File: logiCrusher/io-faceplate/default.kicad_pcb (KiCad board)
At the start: 2 copper layers, 40 x 129 mm, 0 parts

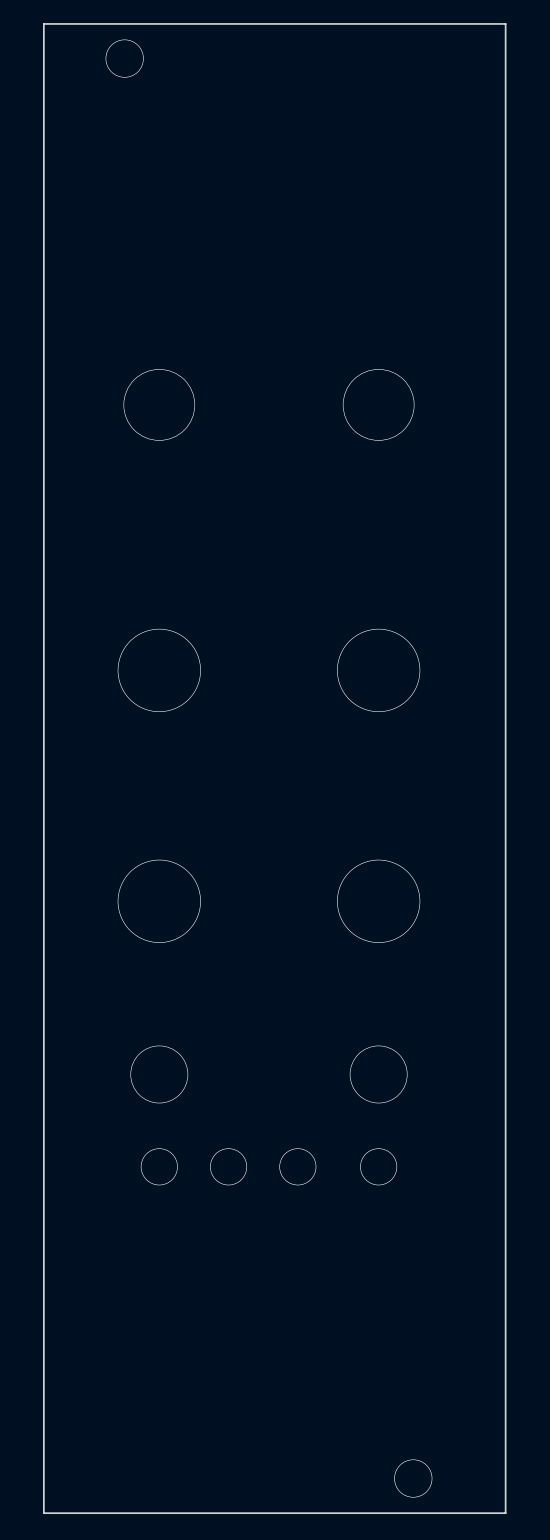
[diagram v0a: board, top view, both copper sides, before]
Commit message: Fit check on the drum and logiccrusher
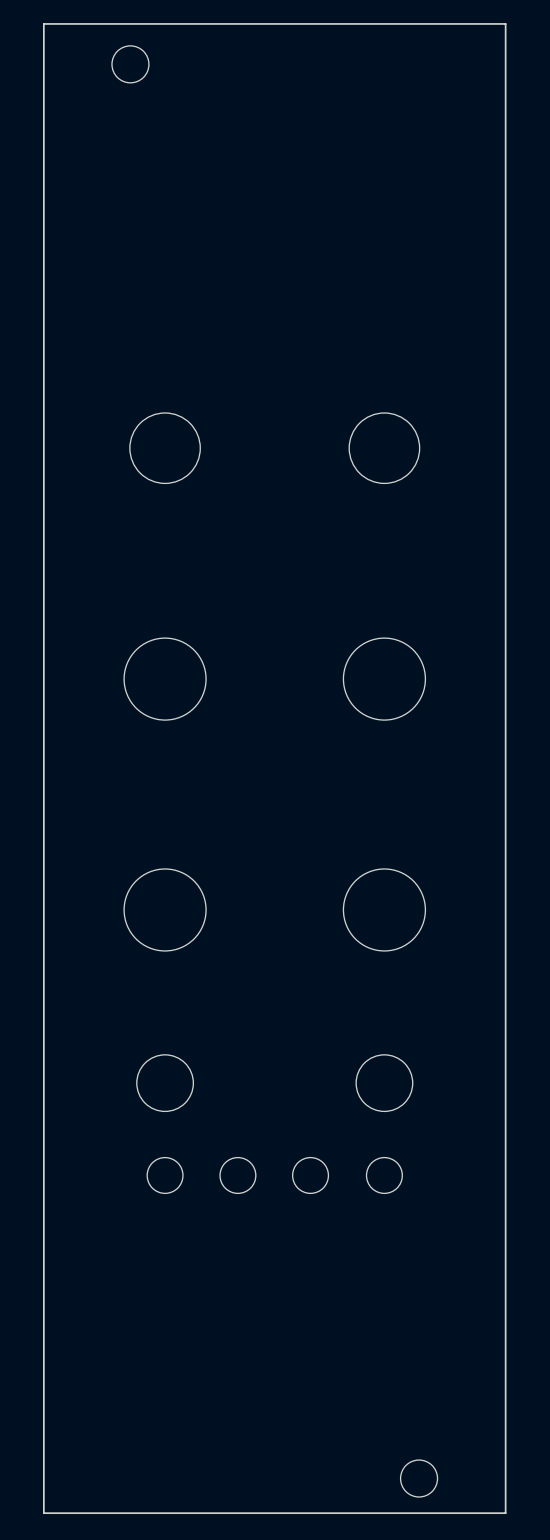
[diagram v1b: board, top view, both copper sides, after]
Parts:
- added ?: , MountingHole:MountingHole_3.5mm, F.Cu at (157.5, 24.5)
- added ?: , MountingHole:MountingHole_3.5mm, F.Cu at (166.8, 120.8)
- added ?: , MountingHole:MountingHole_3.5mm, F.Cu at (173.1, 120.8)
- added ?: , MountingHole:MountingHole_3.5mm, F.Cu at (179.5, 120.8)
- added ?: , MountingHole:MountingHole_3.5mm, F.Cu at (160.5, 112.8)
- added ?: , MountingHole:MountingHole_3.5mm, F.Cu at (179.5, 112.8)
- added ?: , MountingHole:MountingHole_3.5mm, F.Cu at (182.5, 147.0)
- added ?: , MountingHole:MountingHole_3.5mm, F.Cu at (160.5, 97.8)
- added ?: , MountingHole:MountingHole_3.5mm, F.Cu at (179.5, 97.8)
- added ?: , MountingHole:MountingHole_3.5mm, F.Cu at (160.5, 77.8)
- added ?: , MountingHole:MountingHole_3.5mm, F.Cu at (179.5, 77.8)
- added ?: , MountingHole:MountingHole_3.5mm, F.Cu at (160.5, 57.8)
- added ?: , MountingHole:MountingHole_3.5mm, F.Cu at (179.5, 57.8)
- added ?: , MountingHole:MountingHole_3.5mm, F.Cu at (160.5, 120.8)
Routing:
- net (no net): vias 14 -> 0
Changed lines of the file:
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@@
-(kicad_pcb (version 20171130) (host pcbnew 5.0.2+dfsg1-1~bpo9+1)
+(kicad_pcb (version 20171130) (host pcbnew "(5.0.2)-1")
   (general
     (thickness 1.6)
-    (drawings 10)
-    (tracks 14)
+    (drawings 4)
+    (tracks 0)
     (zones 0)
     (modules 0)
@@
       (outputformat 1)
       (mirror false)
-      (drillshape 0)
+      (drillshape 1)
       (scaleselection 1)
-      (outputdirectory "output/"))
+      (outputdirectory ""))
   )
   (net 0 "")
@@
     (uvia_drill 0.1)
   )
-  (gr_line (start 150 150) (end 150 21) (layer Edge.Cuts) (width 0.15))
-  (gr_line (start 150 21) (end 190 21) (layer Edge.Cuts) (width 0.15))
-  (gr_line (start 190 21) (end 190 150) (layer Edge.Cuts) (width 0.15))
-  (gr_line (start 190 150) (end 150 150) (layer Edge.Cuts) (width 0.15))
-  (gr_line (start 150 30) (end 190 30) (layer Dwgs.User) (width 0.15))
-  (gr_line (start 150 140) (end 190 140) (layer Dwgs.User) (width 0.15))
-  (gr_line (start 153 130) (end 153 40) (layer Dwgs.User) (width 0.15))
-  (gr_line (start 153 40) (end 186 40) (layer Dwgs.User) (width 0.15))
-  (gr_line (start 186 40) (end 186 130) (layer Dwgs.User) (width 0.15))
-  (gr_line (start 153 130) (end 186 130) (layer Dwgs.User) (width 0.15))
-  (via (at 157 24) (size 3.3) (drill 3.2) (layers F.Cu B.Cu) (net 0))
-  (via (at 182 147) (size 3.3) (drill 3.2) (layers F.Cu B.Cu) (net 0))
-  (via (at 160 97) (size 7.2) (drill 7.1) (layers F.Cu B.Cu) (net 0))
-  (via (at 179 97) (size 7.2) (drill 7.1) (layers F.Cu B.Cu) (net 0))
-  (via (at 160 77) (size 7.2) (drill 7.1) (layers F.Cu B.Cu) (net 0))
-  (via (at 179 77) (size 7.2) (drill 7.1) (layers F.Cu B.Cu) (net 0))
-  (via (at 160 54) (size 6.2) (drill 6.1) (layers F.Cu B.Cu) (net 0))
-  (via (at 179 54) (size 6.2) (drill 6.1) (layers F.Cu B.Cu) (net 0))
-  (via (at 160 120) (size 3.2) (drill 3.1) (layers F.Cu B.Cu) (net 0))
-  (via (at 166 120) (size 3.2) (drill 3.1) (layers F.Cu B.Cu) (net 0))
-  (via (at 172 120) (size 3.2) (drill 3.1) (layers F.Cu B.Cu) (net 0))
-  (via (at 179 120) (size 3.2) (drill 3.1) (layers F.Cu B.Cu) (net 0))
-  (via (at 160 112) (size 5) (drill 4.9) (layers F.Cu B.Cu) (net 0))
-  (via (at 179 112) (size 5) (drill 4.9) (layers F.Cu B.Cu) (net 0))
+(gr_line (start 150 150) (end 150 21) (layer Edge.Cuts) (width 0.15))
+(gr_line (start 150 21) (end 190 21) (layer Edge.Cuts) (width 0.15))
+(gr_line (start 190 21) (end 190 150) (layer Edge.Cuts) (width 0.15))
+(gr_line (start 190 150) (end 150 150) (layer Edge.Cuts) (width 0.15))
+(module MountingHole:MountingHole_3.5mm (layer F.Cu)
+(at 157.500000 24.500000)
+(pad 1 np_thru_hole circle (at 0 0) (size 3.200000 3.200000) (drill 3.200000) (layers *.Cu *.Mask))
 )
+(module MountingHole:MountingHole_3.5mm (layer F.Cu)
+(at 182.500000 147.000000)
+(pad 1 np_thru_hole circle (at 0 0) (size 3.200000 3.200000) (drill 3.200000) (layers *.Cu *.Mask))
+)
+(gr_line (start 150 30) (end 190 30) (layer Dwgs.User) (width 0.15))
+(gr_line (start 150 140) (end 190 140) (layer Dwgs.User) (width 0.15))
+(gr_line (start 153 130) (end 153 40) (layer Dwgs.User) (width 0.15))
+(gr_line (start 153 40) (end 186 40) (layer Dwgs.User) (width 0.15))
+(gr_line (start 186 40) (end 186 130) (layer Dwgs.User) (width 0.15))
+(gr_line (start 153 130) (end 186 130) (layer Dwgs.User) (width 0.15))
+(module MountingHole:MountingHole_3.5mm (layer F.Cu)
+(at 160.500000 97.750000)
+(pad 1 np_thru_hole circle (at 0 0) (size 7.100000 7.100000) (drill 7.100000) (layers *.Cu *.Mask))
+)
+(module MountingHole:MountingHole_3.5mm (layer F.Cu)
+(at 179.500000 97.750000)
+(pad 1 np_thru_hole circle (at 0 0) (size 7.100000 7.100000) (drill 7.100000) (layers *.Cu *.Mask))
+)
+(module MountingHole:MountingHole_3.5mm (layer F.Cu)
+(at 160.500000 77.750000)
+(pad 1 np_thru_hole circle (at 0 0) (size 7.100000 7.100000) (drill 7.100000) (layers *.Cu *.Mask))
+)
+(module MountingHole:MountingHole_3.5mm (layer F.Cu)
+(at 179.500000 77.750000)
+(pad 1 np_thru_hole circle (at 0 0) (size 7.100000 7.100000) (drill 7.100000) (layers *.Cu *.Mask))
+)
+(module MountingHole:MountingHole_3.5mm (layer F.Cu)
+(at 160.500000 57.750000)
+(pad 1 np_thru_hole circle (at 0 0) (size 6.100000 6.100000) (drill 6.100000) (layers *.Cu *.Mask))
+)
+(module MountingHole:MountingHole_3.5mm (layer F.Cu)
+(at 179.500000 57.750000)
+(pad 1 np_thru_hole circle (at 0 0) (size 6.100000 6.100000) (drill 6.100000) (layers *.Cu *.Mask))
+)
+(module MountingHole:MountingHole_3.5mm (layer F.Cu)
+(at 160.500000 120.750000)
+(pad 1 np_thru_hole circle (at 0 0) (size 3.100000 3.100000) (drill 3.100000) (layers *.Cu *.Mask))
+)
+(module MountingHole:MountingHole_3.5mm (layer F.Cu)
+(at 166.810000 120.750000)
+(pad 1 np_thru_hole circle (at 0 0) (size 3.100000 3.100000) (drill 3.100000) (layers *.Cu *.Mask))
+)
+(module MountingHole:MountingHole_3.5mm (layer F.Cu)
+(at 173.100000 120.750000)
+(pad 1 np_thru_hole circle (at 0 0) (size 3.100000 3.100000) (drill 3.100000) (layers *.Cu *.Mask))
+)
+(module MountingHole:MountingHole_3.5mm (layer F.Cu)
+(at 179.500000 120.750000)
+(pad 1 np_thru_hole circle (at 0 0) (size 3.100000 3.100000) (drill 3.100000) (layers *.Cu *.Mask))
+)
+(module MountingHole:MountingHole_3.5mm (layer F.Cu)
+(at 160.500000 112.750000)
+(pad 1 np_thru_hole circle (at 0 0) (size 4.900000 4.900000) (drill 4.900000) (layers *.Cu *.Mask))
+)
+(module MountingHole:MountingHole_3.5mm (layer F.Cu)
+(at 179.500000 112.750000)
+(pad 1 np_thru_hole circle (at 0 0) (size 4.900000 4.900000) (drill 4.900000) (layers *.Cu *.Mask))
+)
+)

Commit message: pushing those gerbs I was refering to in the last commit
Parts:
- added ?: , , F.Cu at (177.0, 121.0)
- added ?: , , F.Cu at (172.0, 94.0)
- added ?: , , F.Cu at (180.0, 31.0)
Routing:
- net (no net): track 0.00 -> 161.8 mm
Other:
- board text added: "LogiCrusher"
- board text added: "MM MM"
- board text added: "T"
- board text added: "You're on drugs."
